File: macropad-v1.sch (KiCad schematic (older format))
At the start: 24 parts, among them SW1 SW_Push, U1 ATmega32U4-AU, Y1 16MHz

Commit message: pcb routes
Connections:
- net COL0: now also U1.31 (PC6)
- net COL1: now also U1.30 (PB6)
- net ROW0: now also U1.29 (PB5)
- net ROW1: now also U1.32 (PC7)
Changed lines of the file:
@@
 Text GLabel 7225 4600 0    50   Input ~ 0
 ROW1
+Text GLabel 4900 3325 2    50   Input ~ 0
+COL1
+Text GLabel 4900 3225 2    50   Input ~ 0
+ROW0
+Text GLabel 4900 3625 2    50   Input ~ 0
+COL0
+Text GLabel 4900 3725 2    50   Input ~ 0
+ROW1
 $EndSCHEMATC

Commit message: gerber
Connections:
- net GND: now also USB1.6 (SHIELD)
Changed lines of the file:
@@
 Text GLabel 4900 3725 2    50   Input ~ 0
 ROW1
+Wire Wire Line
+	6825 1175 6925 1175
+Wire Wire Line
+	6925 1175 6925 1675
+Connection ~ 6925 1675
 $EndSCHEMATC

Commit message: usb c v1
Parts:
- removed USB1: Molex-0548190589, random-keyboard-parts:Molex-0548190589, symbol random-keyboard-parts:Molex-0548190589
- added D5: PRTR5V0U2X, Package_TO_SOT_SMD:SOT-143, symbol Power_Protection:PRTR5V0U2X
- added J1: USB_C_Receptacle_USB2.0, Connector_USB:USB_C_Receptacle_Amphenol_12401548E4-2A, symbol Connector:USB_C_Receptacle_USB2.0
- added R5, R6: 5.1k, Resistor_SMD:R_0805_2012Metric, symbol Device:R_Small
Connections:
- net D+: now also D5.3 (I/O2), J1.A6 (D+), J1.B6 (D+)
- net D-: now also D5.2 (I/O1), J1.A7 (D-), J1.B7 (D-)
- net GND: now also J1.A1 (GND), J1.A12 (GND), J1.B1 (GND), J1.B12 (GND), J1.S1 (SHIELD)
- net VCC: now also J1.A4 (VBUS), J1.A9 (VBUS), J1.B4 (VBUS), J1.B9 (VBUS)
- new net: J1.A5 (CC1), R5.2
- new net: J1.B5 (CC2), R6.2
- new net: D5.1 (GND), R5.1, R6.1
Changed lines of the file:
@@
 D-
-$Comp
-L random-keyboard-parts:Molex-0548190589 USB1
-U 1 1 5F4FAE8C
-P 6525 1475
-F 0 "USB1" V 7062 1442 60  0000 C CNN
-F 1 "Molex-0548190589" V 6956 1442 60  0000 C CNN
-F 2 "random-keyboard-parts:Molex-0548190589" H 6525 1475 60  0001 C CNN
-F 3 "" H 6525 1475 60  0001 C CNN
-	1    6525 1475
-	0    -1   -1   0
-$EndComp
-$Comp
-L Device:Polyfuse_Small F1
-U 1 1 5F4FEAD4
-P 7550 1275
-F 0 "F1" V 7345 1275 50  0000 C CNN
-F 1 "500mA" V 7436 1275 50  0000 C CNN
-F 2 "Fuse:Fuse_1206_3216Metric" H 7600 1075 50  0001 L CNN
-F 3 "~" H 7550 1275 50  0001 C CNN
-	1    7550 1275
-	0    1    1    0
-$EndComp
-$Comp
-L power:+5V #PWR0111
-U 1 1 5F500AF0
-P 8050 1275
-F 0 "#PWR0111" H 8050 1125 50  0001 C CNN
-F 1 "+5V" H 8065 1448 50  0000 C CNN
-F 2 "" H 8050 1275 50  0001 C CNN
-F 3 "" H 8050 1275 50  0001 C CNN
-	1    8050 1275
-	1    0    0    -1
-$EndComp
-$Comp
-L power:VCC #PWR0112
-U 1 1 5F506E8B
-P 7175 1275
-F 0 "#PWR0112" H 7175 1125 50  0001 C CNN
-F 1 "VCC" H 7190 1448 50  0000 C CNN
-F 2 "" H 7175 1275 50  0001 C CNN
-F 3 "" H 7175 1275 50  0001 C CNN
-	1    7175 1275
-	1    0    0    -1
-$EndComp
-Wire Wire Line
-	8050 1275 7650 1275
-Wire Wire Line
-	7450 1275 7175 1275
-Wire Wire Line
-	7175 1275 6825 1275
-Connection ~ 7175 1275
-Text GLabel 6825 1375 2    50   Input ~ 0
-D-
-Text GLabel 6825 1475 2    50   Input ~ 0
-D+
-$Comp
-L power:GND #PWR0113
-U 1 1 5F50A9D7
-P 6925 1675
-F 0 "#PWR0113" H 6925 1425 50  0001 C CNN
-F 1 "GND" H 6930 1502 50  0000 C CNN
-F 2 "" H 6925 1675 50  0001 C CNN
-F 3 "" H 6925 1675 50  0001 C CNN
-	1    6925 1675
-	1    0    0    -1
-$EndComp
-Wire Wire Line
-	6925 1675 6825 1675
 $Comp
 L Device:D_Small D1
@@
 Text GLabel 4900 3725 2    50   Input ~ 0
 ROW1
-Wire Wire Line
-	6825 1175 6925 1175
-Wire Wire Line
-	6925 1175 6925 1675
-Connection ~ 6925 1675
+$Comp
+L Connector:USB_C_Receptacle_USB2.0 J1
+U 1 1 5F500470
+P 8075 1500
+F 0 "J1" H 8182 2367 50  0000 C CNN
+F 1 "USB_C_Receptacle_USB2.0" H 8182 2276 50  0000 C CNN
+F 2 "Connector_USB:USB_C_Receptacle_Amphenol_12401548E4-2A" H 8225 1500 50  0001 C CNN
+F 3 "https://www.usb.org/sites/default/files/documents/usb_type-c.zip" H 8225 1500 50  0001 C CNN
+	1    8075 1500
+	1    0    0    -1
+$EndComp
+$Comp
+L power:GND #PWR03
+U 1 1 5F502EF6
+P 7925 2400
+F 0 "#PWR03" H 7925 2150 50  0001 C CNN
+F 1 "GND" H 7930 2227 50  0000 C CNN
+F 2 "" H 7925 2400 50  0001 C CNN
+F 3 "" H 7925 2400 50  0001 C CNN
+	1    7925 2400
+	1    0    0    -1
+$EndComp
+Wire Wire Line
+	7775 2400 7925 2400
+Connection ~ 7925 2400
+Wire Wire Line
+	7925 2400 8075 2400
+$Comp
+L power:VCC #PWR01
+U 1 1 5F50505C
+P 8925 900
+F 0 "#PWR01" H 8925 750 50  0001 C CNN
+F 1 "VCC" H 8940 1073 50  0000 C CNN
+F 2 "" H 8925 900 50  0001 C CNN
+F 3 "" H 8925 900 50  0001 C CNN
+	1    8925 900
+	1    0    0    -1
+$EndComp
+$Comp
+L Device:Polyfuse_Small F1
+U 1 1 5F505EC8
+P 9175 900
+F 0 "F1" V 8970 900 50  0000 C CNN
+F 1 "500mA" V 9061 900 50  0000 C CNN
+F 2 "Fuse:Fuse_1206_3216Metric" H 9225 700 50  0001 L CNN
+F 3 "~" H 9175 900 50  0001 C CNN
+	1    9175 900
+	0    1    1    0
+$EndComp
+Wire Wire Line
+	8675 900  8925 900
+Connection ~ 8925 900
+Wire Wire Line
+	8925 900  9075 900
+$Comp
+L power:+5V #PWR02
+U 1 1 5F508A84
+P 9425 900
+F 0 "#PWR02" H 9425 750 50  0001 C CNN
+F 1 "+5V" H 9440 1073 50  0000 C CNN
+F 2 "" H 9425 900 50  0001 C CNN
+F 3 "" H 9425 900 50  0001 C CNN
+	1    9425 900
+	1    0    0    -1
+$EndComp
+Wire Wire Line
+	9275 900  9425 900
+Wire Wire Line
+	8675 1400 8900 1400
+Wire Wire Line
+	8675 1500 8900 1500
+Wire Wire Line
+	8900 1400 8900 1450
+Wire Wire Line
+	8675 1600 8900 1600
+Wire Wire Line
+	8675 1700 8900 1700
+Wire Wire Line
+	8900 1600 8900 1650
+Wire Wire Line
+	8900 1450 8975 1450
+Connection ~ 8900 1450
+Wire Wire Line
+	8900 1450 8900 1500
+Wire Wire Line
+	8900 1650 8975 1650
+Connection ~ 8900 1650
+Wire Wire Line
+	8900 1650 8900 1700
+Text GLabel 8975 1450 2    50   Input ~ 0
+D-
+Text GLabel 8975 1650 2    50   Input ~ 0
+D+
+$Comp
+L Power_Protection:PRTR5V0U2X D5
+U 1 1 5F526AAB
+P 9925 1150
+F 0 "D5" V 9879 1694 50  0000 L CNN
+F 1 "PRTR5V0U2X" V 9970 1694 50  0000 L CNN
+F 2 "Package_TO_SOT_SMD:SOT-143" H 9985 1150 50  0001 C CNN
+F 3 "https://assets.nexperia.com/documents/data-sheet/PRTR5V0U2X.pdf" H 9985 1150 50  0001 C CNN
+	1    9925 1150
+	0    1    1    0
+$EndComp
+$Comp
+L Device:R_Small R5
+U 1 1 5F52842B
+P 9000 1100
+F 0 "R5" V 8925 1025 50  0000 C CNN
+F 1 "5.1k" V 8925 1200 50  0000 C CNN
+F 2 "Resistor_SMD:R_0805_2012Metric" H 9000 1100 50  0001 C CNN
+F 3 "~" H 9000 1100 50  0001 C CNN
+	1    9000 1100
+	0    1    1    0
+$EndComp
+$Comp
+L Device:R_Small R6
+U 1 1 5F529414
+P 9000 1200
+F 0 "R6" V 9075 1125 50  0000 C CNN
+F 1 "5.1k" V 9075 1300 50  0000 C CNN
+F 2 "Resistor_SMD:R_0805_2012Metric" H 9000 1200 50  0001 C CNN
+F 3 "~" H 9000 1200 50  0001 C CNN
+	1    9000 1200
+	0    1    1    0
+$EndComp
+Wire Wire Line
+	8675 1100 8900 1100
+Wire Wire Line
+	8675 1200 8900 1200
+Wire Wire Line
+	9100 1100 9200 1100
+Wire Wire Line
+	9200 1100 9200 1150
+Wire Wire Line
+	9200 1200 9100 1200
+Wire Wire Line
+	9200 1150 9425 1150
+Connection ~ 9200 1150
+Wire Wire Line
+	9200 1150 9200 1200
+Text GLabel 9925 650  1    50   Input ~ 0
+D-
+Text GLabel 9925 1650 3    50   Input ~ 0
+D+
 $EndSCHEMATC

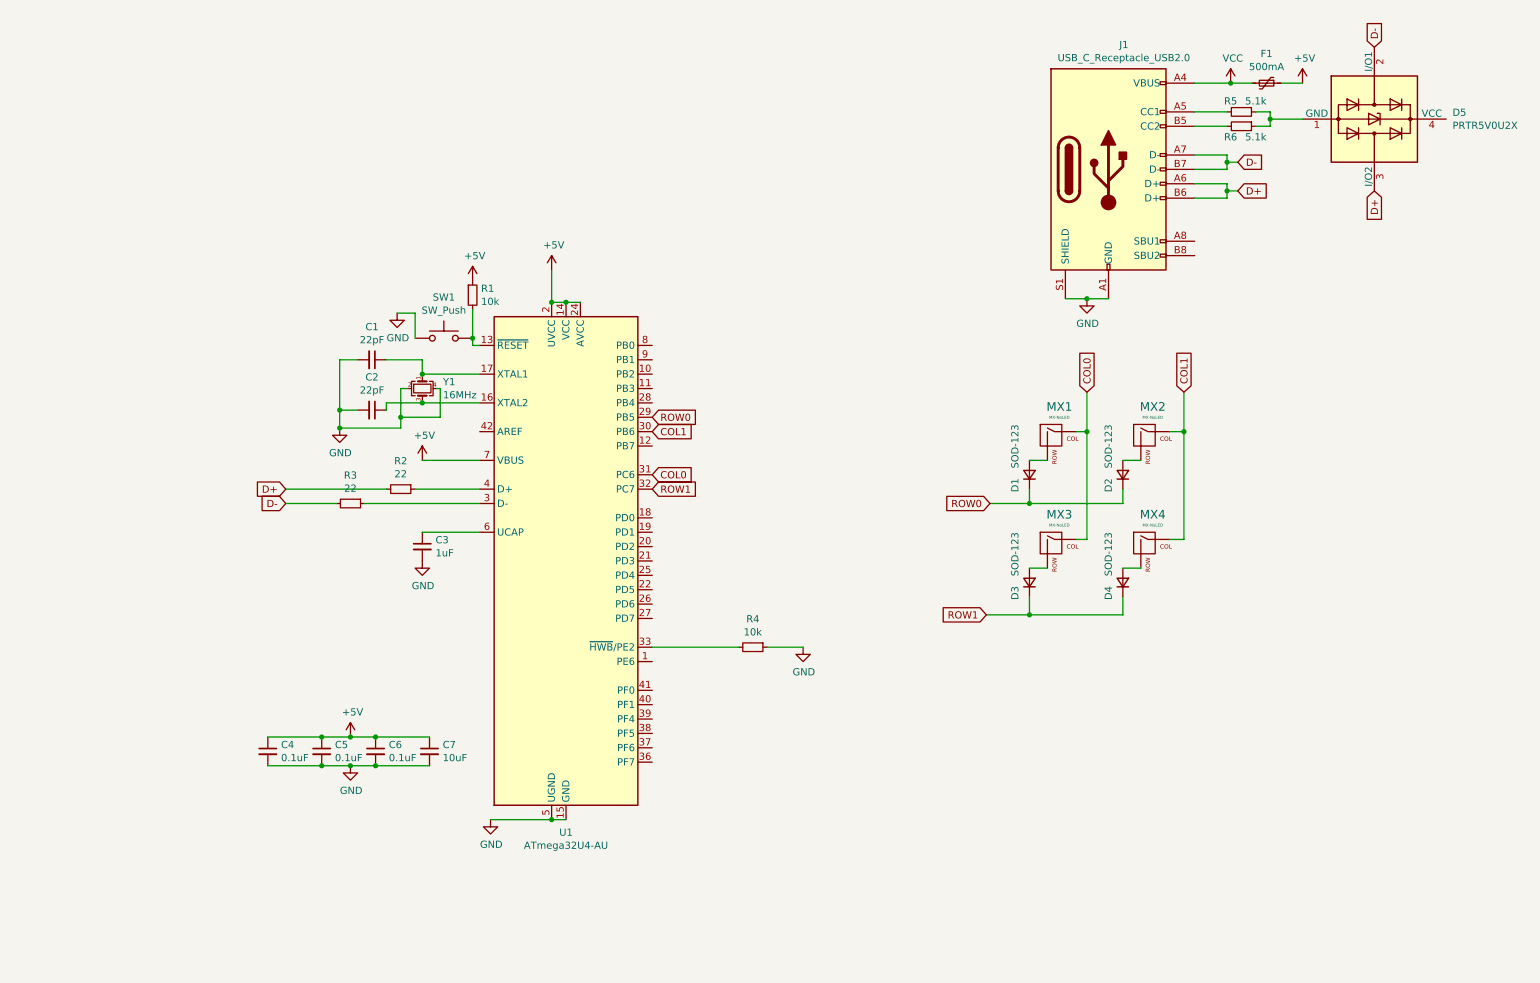
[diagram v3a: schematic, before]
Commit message: usb c and better routing
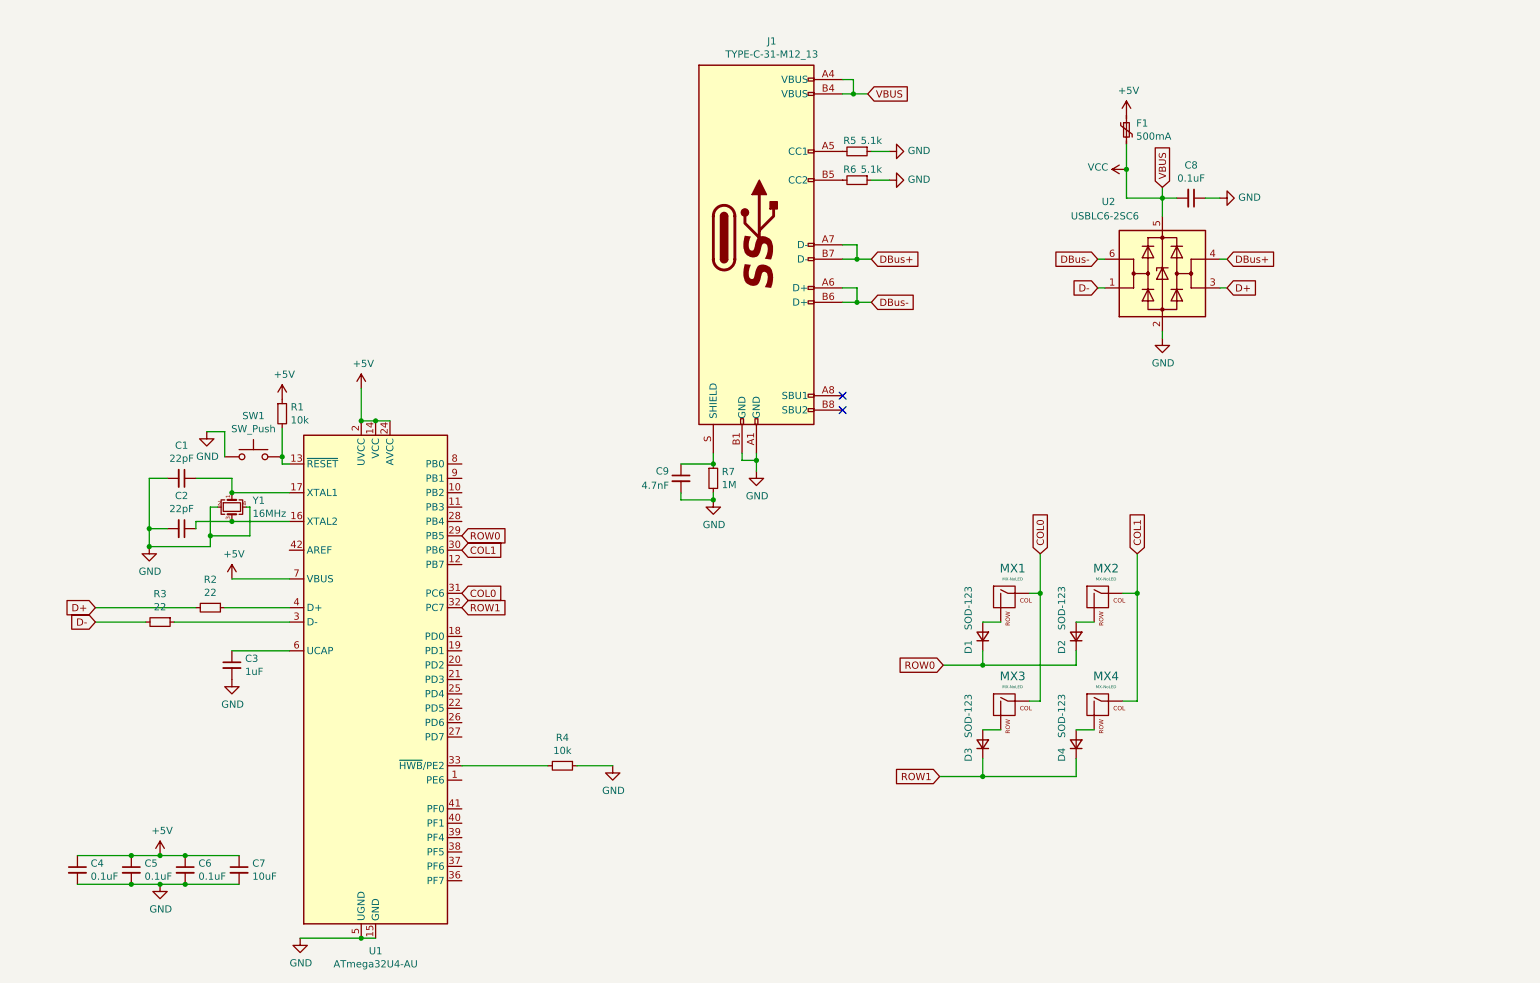
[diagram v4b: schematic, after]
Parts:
- removed D5: PRTR5V0U2X, Package_TO_SOT_SMD:SOT-143, symbol Power_Protection:PRTR5V0U2X
- removed J1: USB_C_Receptacle_USB2.0, Connector_USB:USB_C_Receptacle_Amphenol_12401548E4-2A, symbol Connector:USB_C_Receptacle_USB2.0
- added C8: 0.1uF, Capacitor_SMD:C_0805_2012Metric, symbol Device:C_Small
- added C9: 4.7nF, Capacitor_SMD:C_0805_2012Metric, symbol Device:C_Small
- added J1: TYPE-C-31-M12_13, acheron_Connectors:TYPE-C-31-M-12, symbol acheronSymbols:TYPE-C-31-M12_13
- added R7: 1M, Resistor_SMD:R_0805_2012Metric, symbol Device:R_Small
- added U2: USBLC6-2SC6, Package_TO_SOT_SMD:SOT-23-6, symbol Power_Protection:USBLC6-2SC6
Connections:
- net D+: now also U2.3 (I/O2)
- net D-: now also U2.1 (I/O1)
- net GND: now also R5.1, R6.1, C8.1, C9.2, J1.A1 (GND), J1.B1 (GND), R7.2, U2.2 (GND)
- net VCC: now also C8.2, J1.A4 (VBUS), J1.B4 (VBUS), U2.5 (VBUS)
- net at R5.2: now also J1.A5 (CC1)
- net at R6.2: now also J1.B5 (CC2)
- new net: C9.1, J1.S (SHIELD), R7.1
- new net DBus+: J1.A7 (D-), J1.B7 (D-), U2.4 (I/O2)
- new net DBus-: J1.A6 (D+), J1.B6 (D+), U2.6 (I/O1)
- no-connect marks 0 -> 2
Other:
- moved on the sheet: C1, C2, C3, C4, C5, C6, C7, D1, D2, D3, D4, MX1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

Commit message: RGB
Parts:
- added D? (x4): WS2812B, LED_SMD:LED_WS2812B_PLCC4_5.0x5.0mm_P3.2mm, symbol LED:WS2812B
- added LED? (x4): LED, symbol acheronSymbols:LED
- added Q?: AO4406AL, symbol acheronSymbols:AO4406AL
- added R? (x4): 360, symbol Device:R_Small
- added R?: 100, symbol Device:R_Small
- added R?: 10k, symbol Device:R_Small
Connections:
- net +5V: now also D?.1 (VDD), D?.1 (VDD), D?.1 (VDD), D?.1 (VDD), R?.1, R?.1, R?.1, R?.1
- net GND: now also D?.3 (VSS), D?.3 (VSS), D?.3 (VSS), D?.3 (VSS), Q?.1, Q?.2, Q?.3, R?.2
- net RGB_PWM: now reaches U1.27 (PD7)
- net RGB_PWM: now also D?.4 (DIN), D?.4 (DIN)
- net LED_PWM: now reaches U1.28 (PB4)
- net LED_PWM: now also R?.2
- new net: D?.2 (DOUT), D?.4 (DIN) (x2)
- new net: LED?.A, R?.2 (x4)
- new net: LED?.K, LED?.K, LED?.K, LED?.K, Q?.5 (D), Q?.6, Q?.7, Q?.8
- new net: Q?.4 (G), R?.1, R?.1
